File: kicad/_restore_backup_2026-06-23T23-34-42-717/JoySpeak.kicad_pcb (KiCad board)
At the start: 4 copper layers, 95.7 x 60.9 mm, 62 parts, among them CN1 AUDIO_IN, CN2 AUDIO_OUT, J1 Hexpansion-Connector, J3 Conn_01x02_Pin, J4 GPIO1, J5 Conn_01x02_Pin, SW1 TS-1187A-B-A-B, SW2 TS-1187A-B-A-B, U1 TLV320AIC3100, U2 YV13S-L7.85-B10KA(60)-0-DL01, U3 RP2040-ZERO, U4 AMS1117-1.8

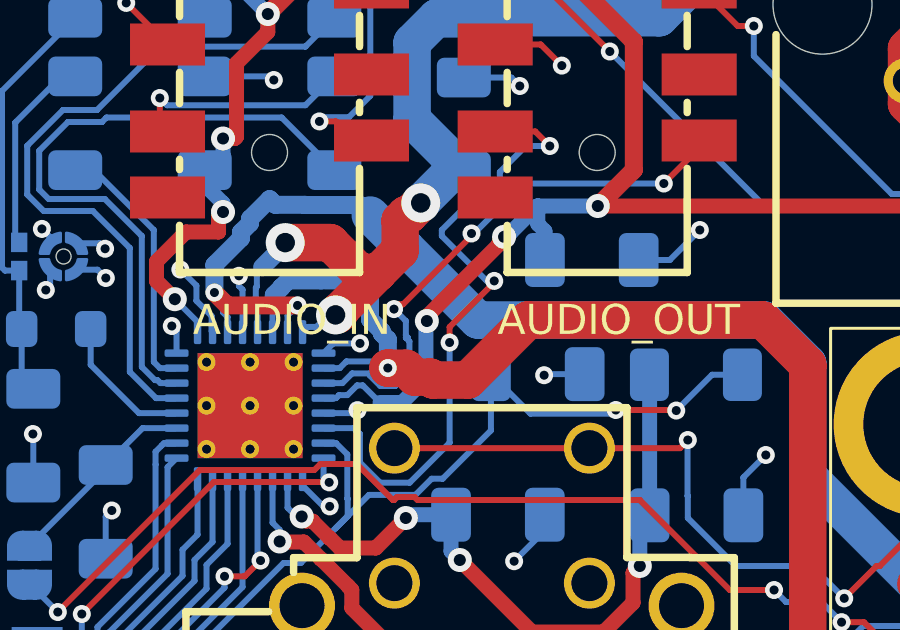
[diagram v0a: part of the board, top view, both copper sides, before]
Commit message: Finalised, pass DFM and sent for fabrication (JLCPCB)
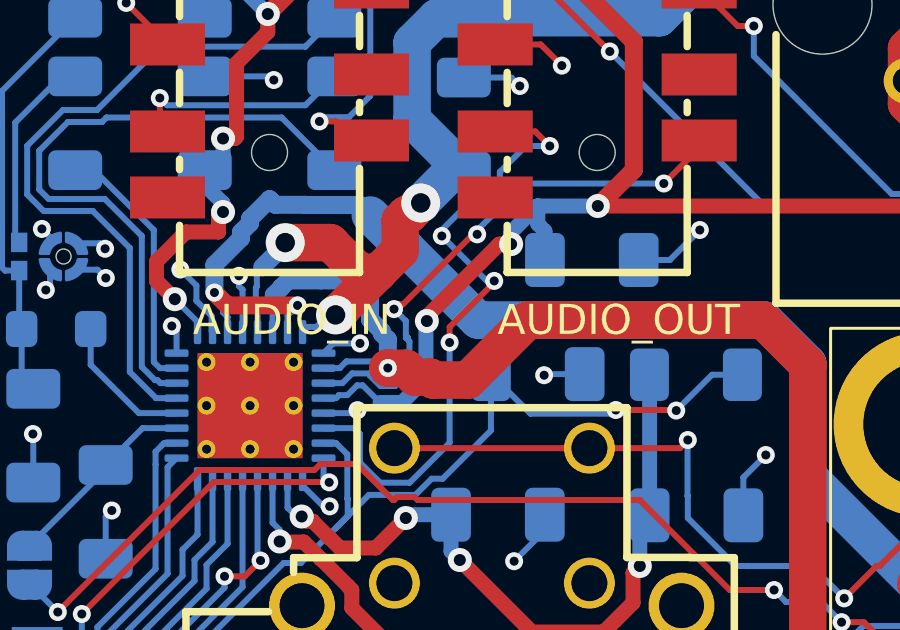
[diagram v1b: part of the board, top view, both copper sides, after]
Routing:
- net /AUD_OUT_R: vias 3 -> 4
